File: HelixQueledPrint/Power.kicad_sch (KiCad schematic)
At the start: 20 parts, among them J601 Screw_Terminal_01x02, U601 MB34F, U602 SY8366H

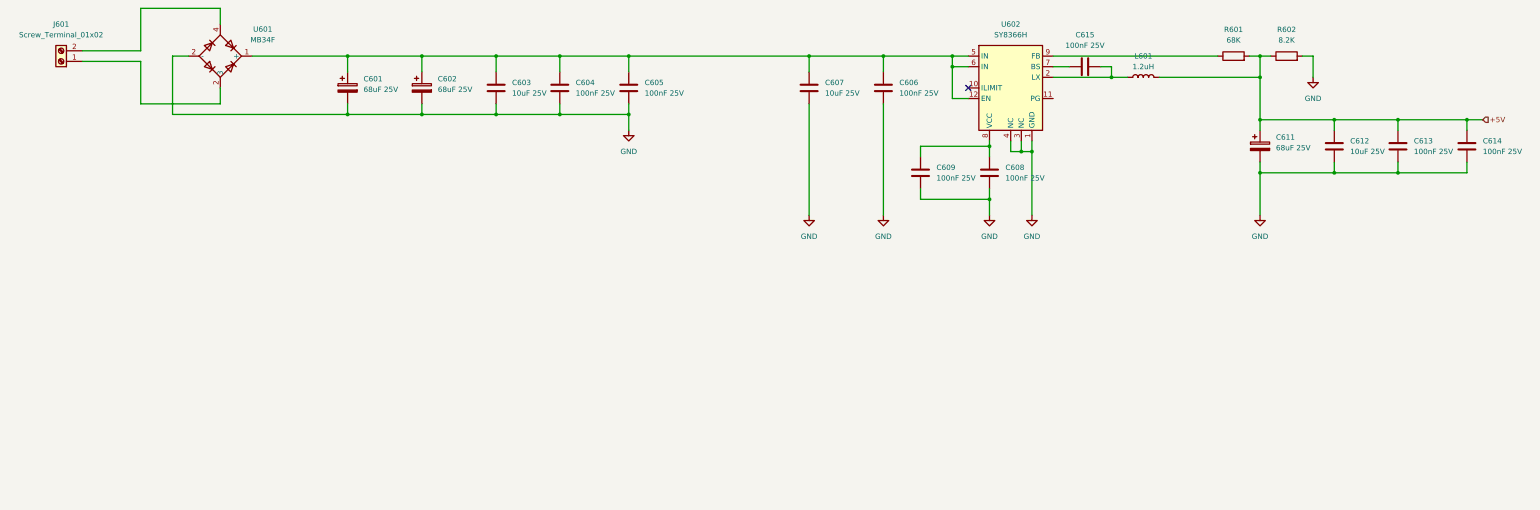
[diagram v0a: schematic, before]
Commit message: 3.3V voeding toegevoegd
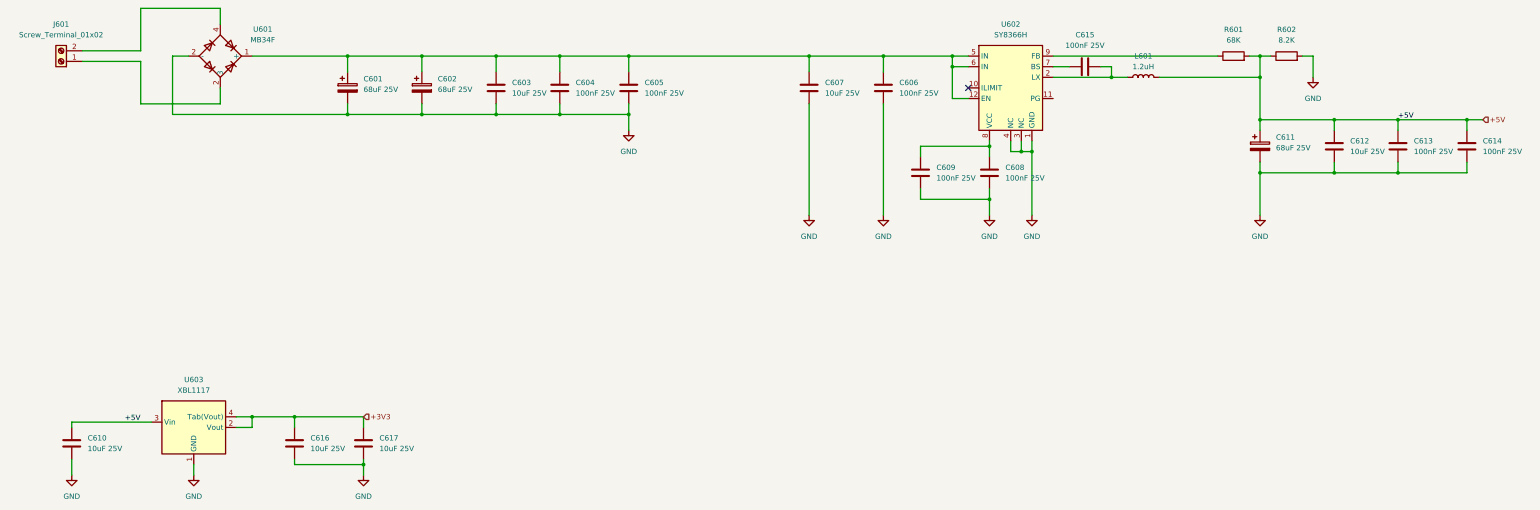
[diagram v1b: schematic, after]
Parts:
- added C610, C616, C617: 10uF 25V, Capacitor_SMD:C_0805_2012Metric, symbol Device:C
- added U603: XBL1117, symbol customFootprints:XBL1117-xx/STR
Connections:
- net +5V: now also C610.1, U603.3 (Vin)
- net GND: now also C610.2, C616.2, C617.2, U603.1 (GND)
- new net +3V3: C616.1, C617.1, U603.2 (Vout), U603.4 (Tab(Vout))

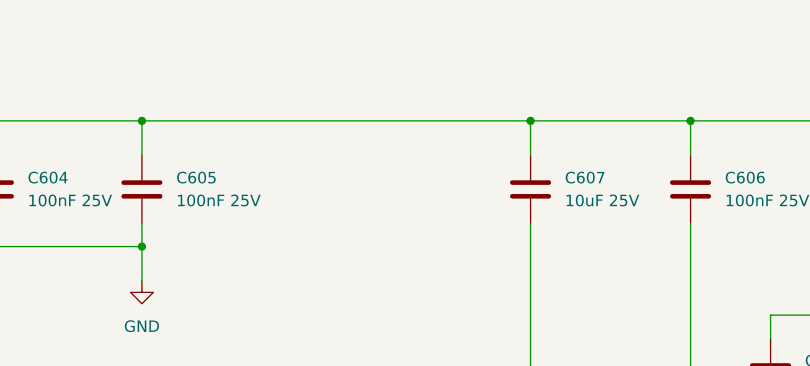
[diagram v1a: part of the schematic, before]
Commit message: GPIO verbindingen gemaakt, en condensatoren toegevoegd
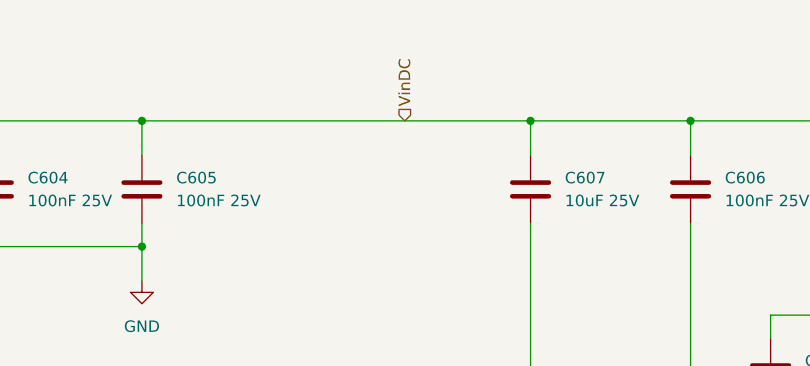
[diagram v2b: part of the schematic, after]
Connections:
- net VinDC: now reaches C601.1, C602.1, C603.1, C604.1, C605.1, C606.1, C607.1, U601.1 (+), U602.12 (EN), U602.5 (IN), U602.6 (IN)
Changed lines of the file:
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@@
+		)
+	)
+	(hierarchical_label "VinDC"
+		(shape input)
+		(at 193.04 63.5 90)
+		(effects
+			(font
+				(size 1.27 1.27)
+			)
+			(justify left)
 		)
 	)

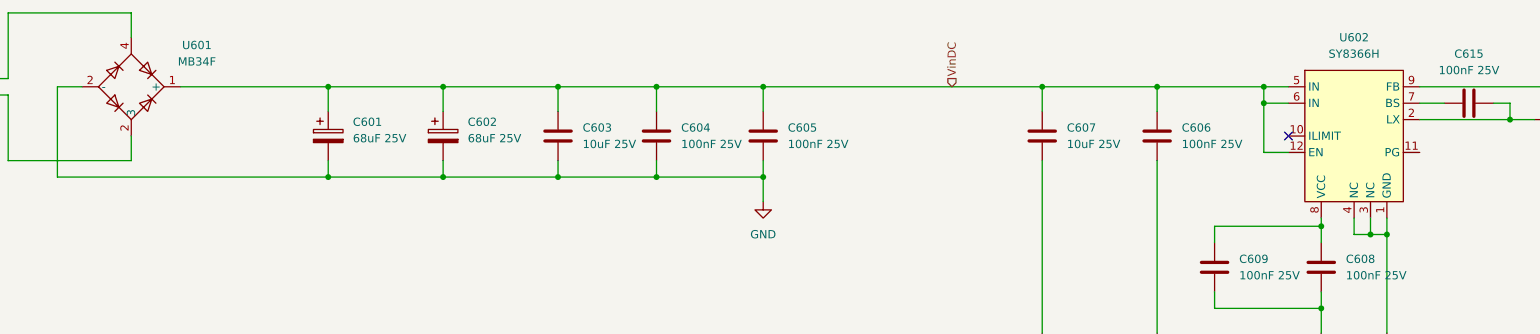
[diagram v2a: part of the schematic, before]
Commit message: footprints toegewezen
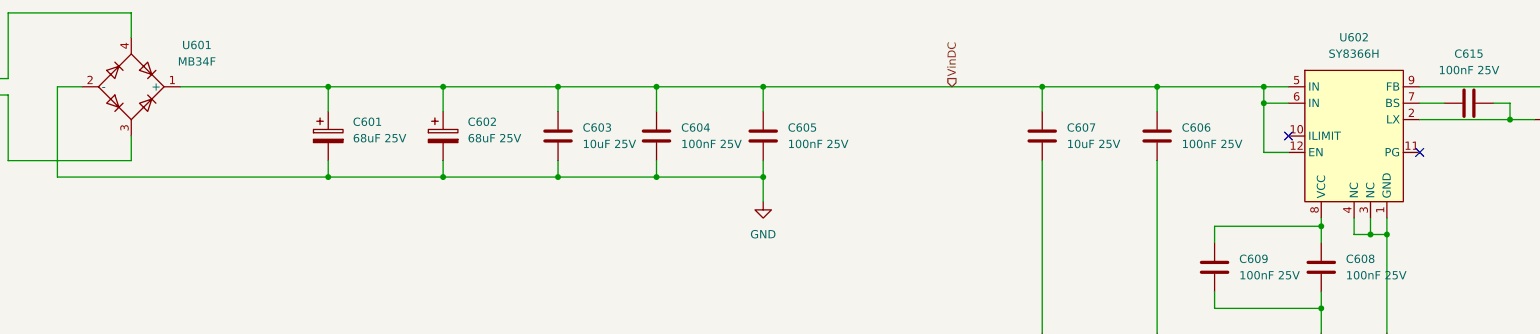
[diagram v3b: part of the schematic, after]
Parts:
- C601, C602, C611: footprint (none) -> Capacitor_SMD:CP_Elec_6.3x5.4; MPN (none) -> CS1E680M-CRE54
- J601: footprint (none) -> TerminalBlock:TerminalBlock_Xinya_XY308-2.54-2P_1x02_P2.54mm_Horizontal; MPN (none) -> MX128-2.54-02P-GN01-Cu-Y-A
- L601: footprint (none) -> Inductor_SMD:L_APV_ANR4012; MPN C149536 -> FTC404020S1R2MBCA
- U601: footprint (none) -> 1CustomFootprints:MFB; symbol customFootprints:GOODWORK MB34F -> 1CustomSymbols:GOODWORK MB34F
- U602: footprint (none) -> 1CustomFootprints:QFN3X3-12_SGY
- U603: footprint (none) -> Package_TO_SOT_SMD:SOT-223; MPN (none) -> XBLW XBL1117-3.3
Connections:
- net at J601.1 (Pin_1): now also U601.3; no longer U601.2 (3)
- no-connect marks 1 -> 2
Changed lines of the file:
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@@
 		(at 245.11 71.12)
 	)
+	(no_connect
+		(at 265.43 73.66)
+	)
 	(wire
 		(pts
@@
 			)
 		)
-		(property "Footprint" ""
+		(property "Footprint" "Package_TO_SOT_SMD:SOT-223"
 			(at 59.69 152.4 0)
 			(effects
@@
 			)
 		)
+		(property "MPN" "XBLW XBL1117-3.3"
+			(at 59.69 152.4 0)
+			(effects
+				(font
+					(size 1.27 1.27)
+				)
+				(hide yes)
+			)
+		)
 		(pin "3"
 		)
@@
 			)
 		)
-		(property "Footprint" ""
+		(property "Footprint" "Inductor_SMD:L_APV_ANR4012"
 			(at 287.02 68.58 0)
 			(effects
@@
 			)
 		)
-		(property "MPN" "C149536"
+		(property "MPN" "FTC404020S1R2MBCA"
 			(at 287.02 68.58 90)
 			(effects
@@
 			)
 		)
-		(property "Footprint" ""
+		(property "Footprint" "Capacitor_SMD:CP_Elec_6.3x5.4"
 			(at 115.2652 74.93 0)
 			(effects
@@
 			)
 		)
+		(property "MPN" "CS1E680M-CRE54 "
+			(at 114.3 71.12 0)
+			(effects
+				(font
+					(size 1.27 1.27)
+				)
+				(hide yes)
+			)
+		)
 		(pin "2"
 		)
@@
 			)
 		)
-		(property "Footprint" ""
+		(property "Footprint" "TerminalBlock:TerminalBlock_Xinya_XY308-2.54-2P_1x02_P2.54mm_Horizontal"
 			(at 27.94 64.77 0)
 			(effects
@@
 			)
 		)
+		(property "MPN" "MX128-2.54-02P-GN01-Cu-Y-A "
+			(at 27.94 64.77 0)
+			(effects
+				(font
+					(size 1.27 1.27)
+				)
+				(hide yes)
+			)
+		)
 		(pin "1"
 		)
@@
 	)
 	(symbol
-		(lib_id "customFootprints:GOODWORK MB34F")
+		(lib_id "1CustomSymbols:GOODWORK MB34F")
 		(at 66.04 63.5 0)
 		(unit 1)
@@
 			)
 		)
-		(property "Footprint" ""
+		(property "Footprint" "1CustomFootprints:MFB"
 			(at 66.04 63.5 0)
 			(effects
@@
 			)
 		)
-		(property "Description" ""
+		(property "Description" "Full bridge rectifier 200V 3A"
 			(at 66.04 63.5 0)
 			(effects
@@
 		(pin "2"
 		)
-		(pin "2"
+		(pin "3"
 		)
 		(instances
@@
 			)
 		)
-		(property "Footprint" ""
+		(property "Footprint" "Capacitor_SMD:CP_Elec_6.3x5.4"
 			(at 315.9252 88.9 0)
 			(effects
@@
 			)
 		)
+		(property "MPN" "CS1E680M-CRE54 "
+			(at 314.96 85.09 0)
+			(effects
+				(font
+					(size 1.27 1.27)
+				)
+				(hide yes)
+			)
+		)
 		(pin "2"
 		)
@@
 			)
 		)
-		(property "Footprint" ""
+		(property "Footprint" "Capacitor_SMD:CP_Elec_6.3x5.4"
 			(at 97.4852 74.93 0)
 			(effects
@@
 			)
 		)
+		(property "MPN" "CS1E680M-CRE54 "
+			(at 96.52 71.12 0)
+			(effects
+				(font
+					(size 1.27 1.27)
+				)
+				(hide yes)
+			)
+		)
 		(pin "2"
 		)
@@
 			)
 		)
-		(property "Footprint" ""
+		(property "Footprint" "1CustomFootprints:QFN3X3-12_SGY"
 			(at 255.27 71.12 0)
 			(effects
